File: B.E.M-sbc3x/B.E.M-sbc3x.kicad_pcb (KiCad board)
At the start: 2 copper layers, 7 parts, among them J1 Screw_Terminal_01x02, U1 6822, U2 6822, U3 MC68A09, U4 TC55257PL-12, U5 27256, U6 DM74S571

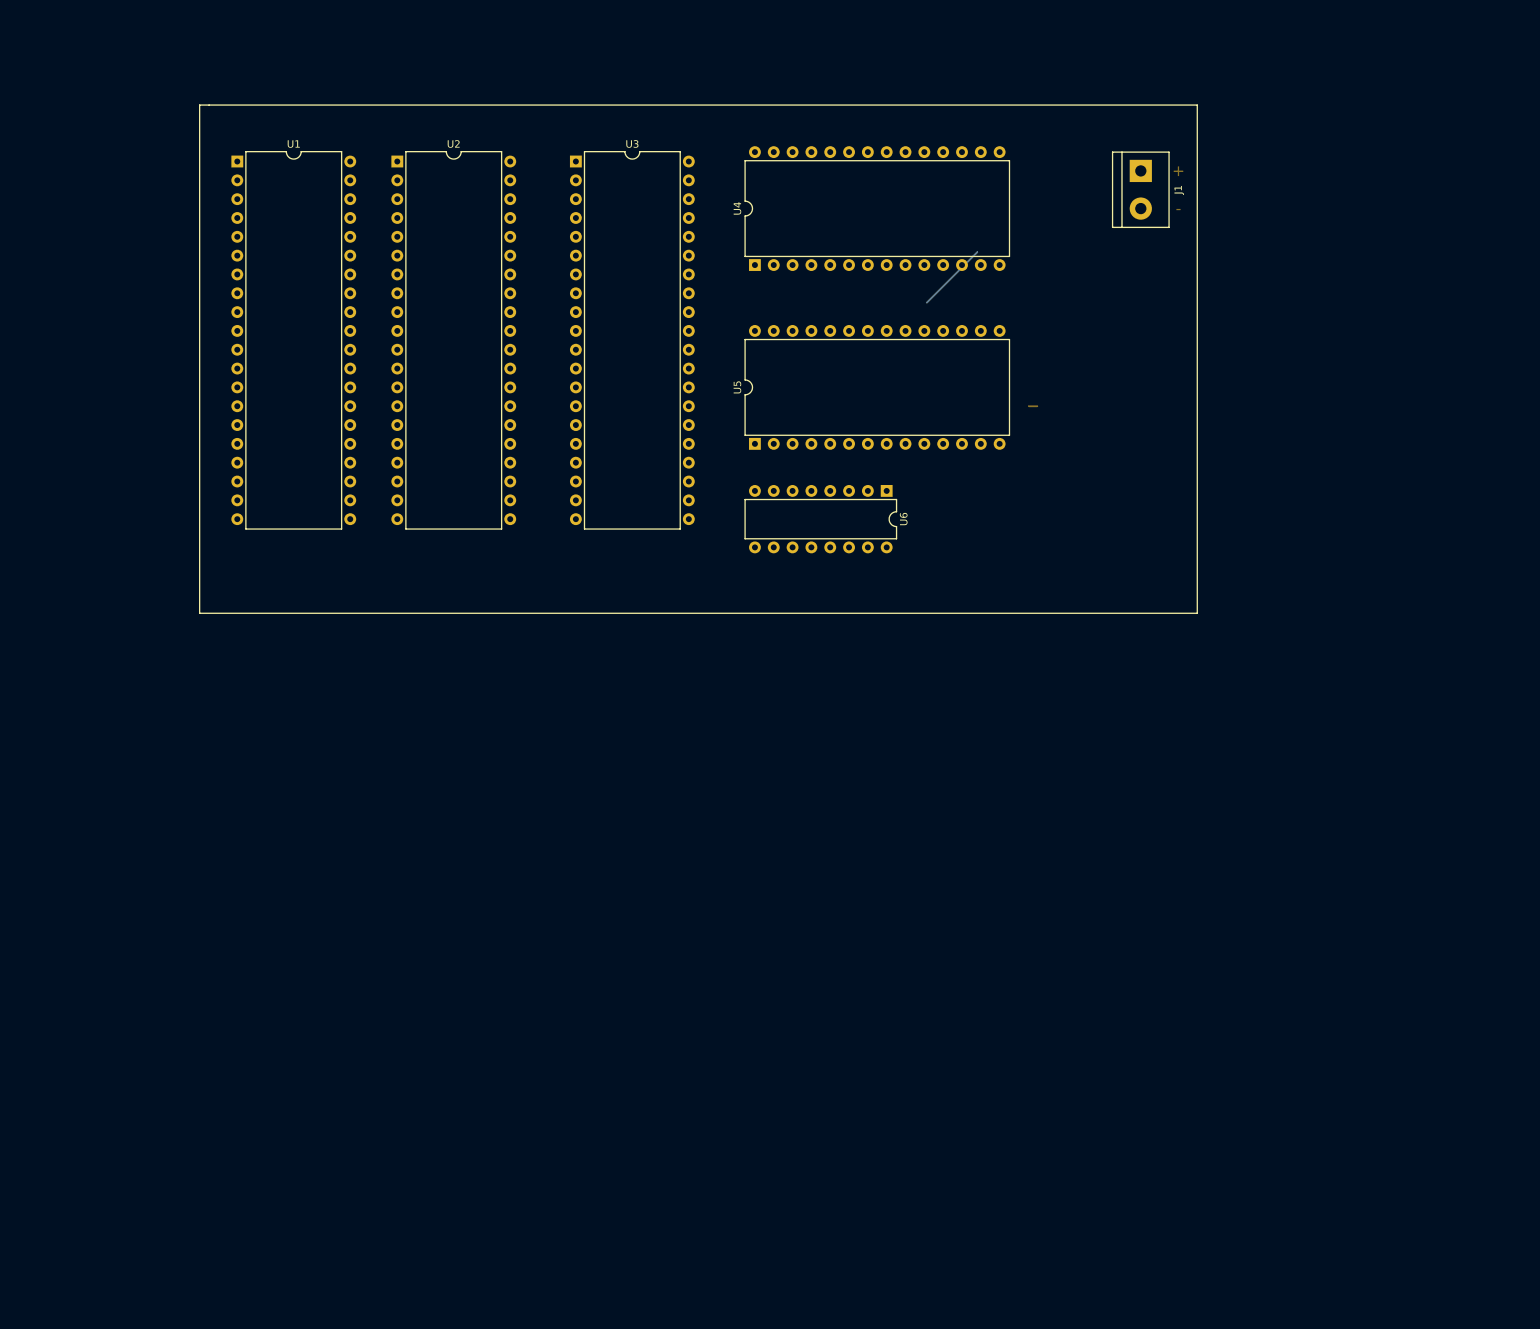
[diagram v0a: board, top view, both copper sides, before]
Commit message: Almost finnished with the schema and layout. Only some jumpers are not yet mapped out. For the PCB layout is only component placement is done, no routing
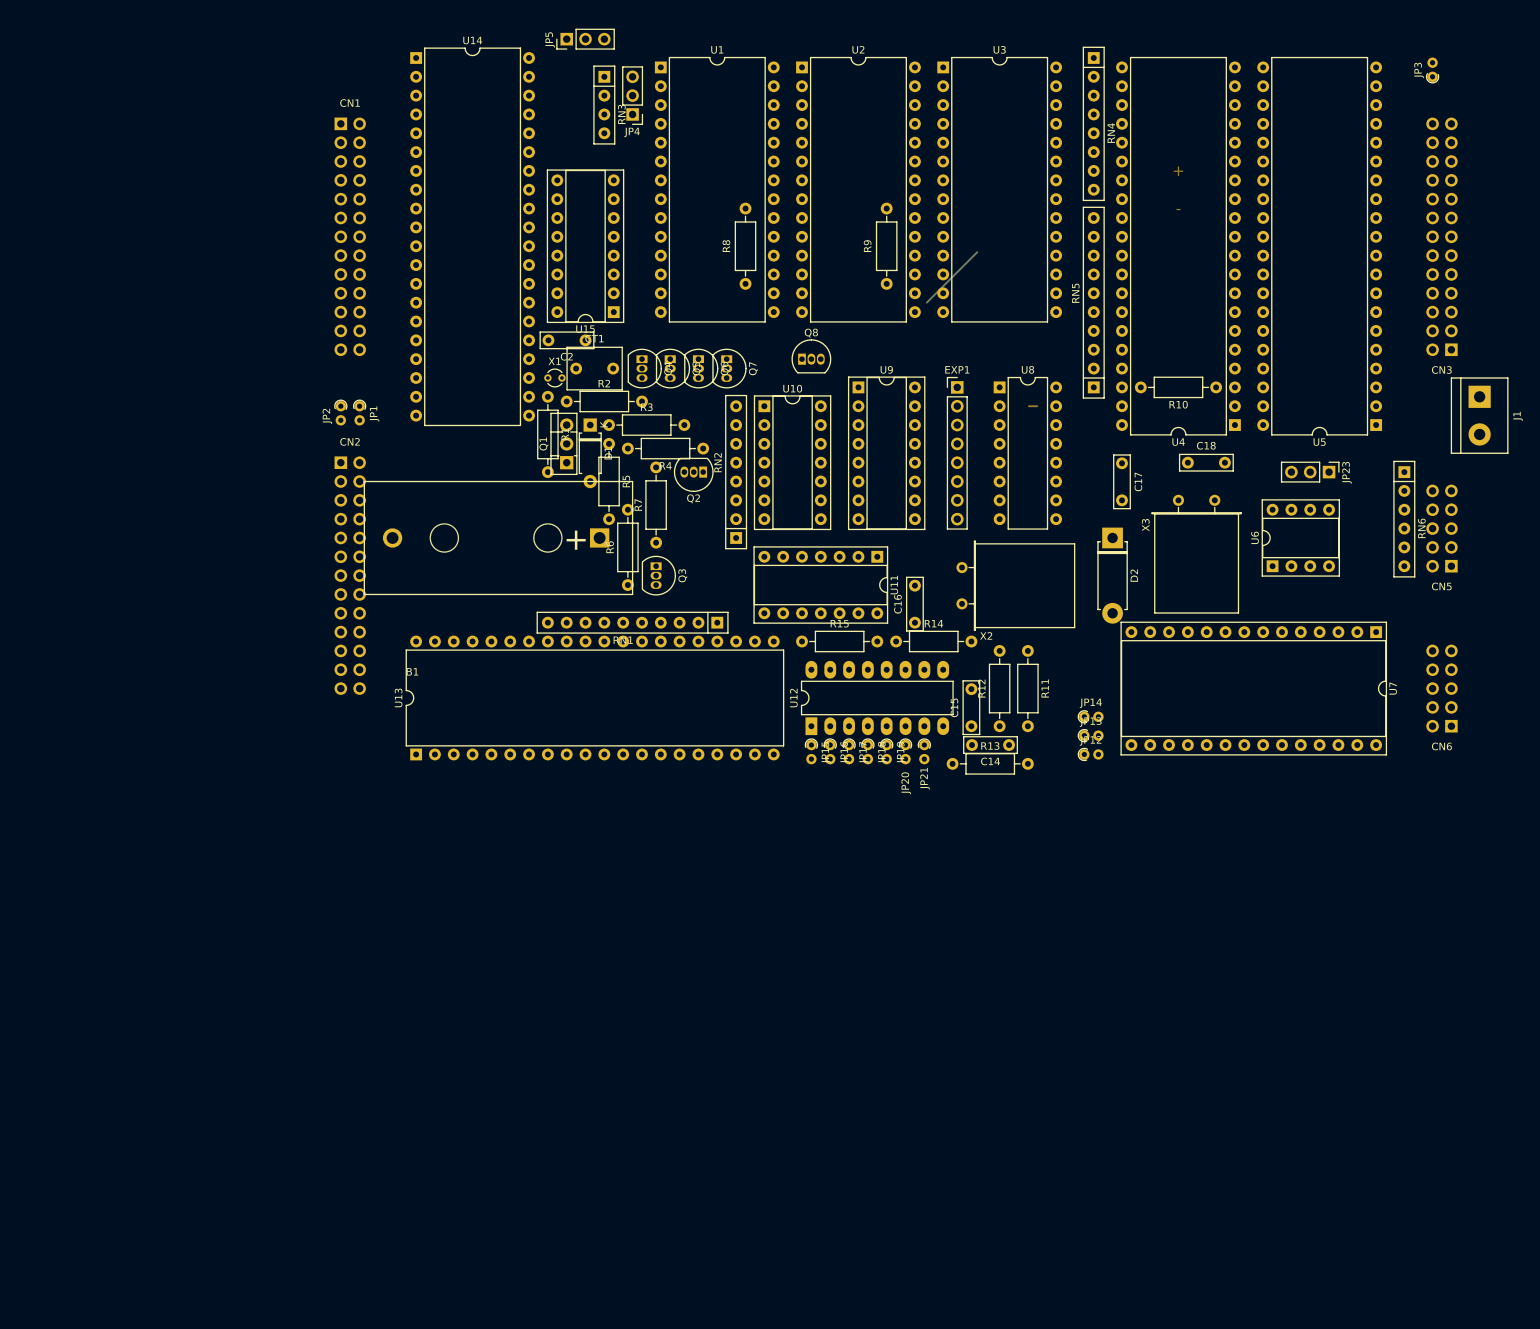
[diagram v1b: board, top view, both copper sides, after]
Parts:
- added B1: Battery_Cell, B.E.M:Battery_3.6v, F.Cu at (104.8, 90.2)
- added C14: 100n, Capacitor_THT:C_Rect_L7.0mm_W2.0mm_P5.00mm, F.Cu at (157.5, 118.1)
- added C15: 10n, Capacitor_THT:C_Rect_L7.0mm_W2.0mm_P5.00mm, F.Cu at (152.4, 115.6)
- added C16: 100pF, Capacitor_THT:C_Rect_L7.0mm_W2.0mm_P5.00mm, F.Cu at (144.8, 101.6)
- added C17: 22p, Capacitor_THT:C_Rect_L7.0mm_W2.0mm_P5.00mm, F.Cu at (172.7, 80.1)
- added C18: 22p, Capacitor_THT:C_Rect_L7.0mm_W2.0mm_P5.00mm, F.Cu at (181.6, 80.0)
- added C2: 22P, Capacitor_THT:C_Rect_L7.0mm_W2.0mm_P5.00mm, F.Cu at (100.3, 63.5)
- added CN1: Conn_02x13_Odd_Even, Connector_PinSocket_2.54mm:PinSocket_2x13_P2.54mm_Vertical, B.Cu at (67.3, 34.3)
- added CN2: Conn_02x13_Odd_Even, Connector_PinSocket_2.54mm:PinSocket_2x13_P2.54mm_Vertical, B.Cu at (67.3, 80.0)
- added CN3: Conn_02x13_Odd_Even, Connector_PinSocket_2.54mm:PinSocket_2x13_P2.54mm_Vertical, B.Cu at (217.2, 64.8)
- added CN5: Conn_02x05_Odd_Even, Connector_PinSocket_2.54mm:PinSocket_2x05_P2.54mm_Vertical, B.Cu at (217.2, 94.0)
- added CN6: Conn_02x05_Odd_Even, Connector_PinSocket_2.54mm:PinSocket_2x05_P2.54mm_Vertical, B.Cu at (217.2, 115.6)
- added CT1: 30pF, Capacitor_THT:C_Rect_L7.2mm_W5.5mm_P5.00mm_FKS2_FKP2_MKS2_MKP2, F.Cu at (99.1, 67.3)
- added D1: 1N4148, Diode_THT:D_A-405_P7.62mm_Horizontal, F.Cu at (101.0, 74.9)
- added D2: 1N4148, Diode_THT:D_5W_P10.16mm_Horizontal, F.Cu at (171.4, 90.2)
- added EXP1: Exp, Connector_PinHeader_2.54mm:PinHeader_1x08_P2.54mm_Vertical, F.Cu at (150.5, 69.8)
- added JP1: Jumper_NO_Small, Resistor_THT:R_Axial_DIN0204_L3.6mm_D1.6mm_P1.90mm_Vertical, F.Cu at (69.8, 72.4)
- added JP12: Jumper_NO_Small, Resistor_THT:R_Axial_DIN0204_L3.6mm_D1.6mm_P1.90mm_Vertical, F.Cu at (167.6, 119.4)
- added JP13: Jumper_NO_Small, Resistor_THT:R_Axial_DIN0204_L3.6mm_D1.6mm_P1.90mm_Vertical, F.Cu at (167.6, 116.8)
- added JP14: Jumper_NO_Small, Resistor_THT:R_Axial_DIN0204_L3.6mm_D1.6mm_P1.90mm_Vertical, F.Cu at (167.6, 114.3)
- added JP15: Jumper_NO_Small, Resistor_THT:R_Axial_DIN0204_L3.6mm_D1.6mm_P1.90mm_Vertical, F.Cu at (130.8, 118.1)
- added JP16: Jumper_NO_Small, Resistor_THT:R_Axial_DIN0204_L3.6mm_D1.6mm_P1.90mm_Vertical, F.Cu at (133.3, 118.1)
- added JP17: Jumper_NO_Small, Resistor_THT:R_Axial_DIN0204_L3.6mm_D1.6mm_P1.90mm_Vertical, F.Cu at (135.9, 118.1)
- added JP18: Jumper_NO_Small, Resistor_THT:R_Axial_DIN0204_L3.6mm_D1.6mm_P1.90mm_Vertical, F.Cu at (138.4, 118.1)
- added JP19: Jumper_NO_Small, Resistor_THT:R_Axial_DIN0204_L3.6mm_D1.6mm_P1.90mm_Vertical, F.Cu at (141.0, 118.1)
- added JP2: Jumper_NO_Small, Resistor_THT:R_Axial_DIN0204_L3.6mm_D1.6mm_P1.90mm_Vertical, F.Cu at (67.3, 72.4)
- added JP20: Jumper_NO_Small, Resistor_THT:R_Axial_DIN0204_L3.6mm_D1.6mm_P1.90mm_Vertical, F.Cu at (143.5, 118.1)
- added JP21: Jumper_NO_Small, Resistor_THT:R_Axial_DIN0204_L3.6mm_D1.6mm_P1.90mm_Vertical, F.Cu at (146.1, 118.1)
- added JP23: Jumper_3_Open, Connector_PinHeader_2.54mm:PinHeader_1x03_P2.54mm_Vertical, F.Cu at (200.7, 81.3)
- added JP3: Jumper_NO_Small, Resistor_THT:R_Axial_DIN0204_L3.6mm_D1.6mm_P1.90mm_Vertical, F.Cu at (214.6, 27.9)
- added JP4: Jumper_3_Open, Connector_PinHeader_2.54mm:PinHeader_1x03_P2.54mm_Vertical, F.Cu at (106.7, 33.0)
- added JP5: Jumper_3_Open, Connector_PinHeader_2.54mm:PinHeader_1x03_P2.54mm_Vertical, F.Cu at (97.8, 22.9)
- added Q1: BD136, Package_TO_SOT_THT:TO-126-3_Vertical, F.Cu at (97.8, 80.0)
- added Q2: BC556, Package_TO_SOT_THT:TO-92_Inline, F.Cu at (116.2, 81.3)
- added Q3: BC547, Package_TO_SOT_THT:TO-92_Inline, F.Cu at (109.9, 94.0)
- added Q4: BC547, Package_TO_SOT_THT:TO-92_Inline, F.Cu at (108.0, 66.0)
- added Q5: BC547, Package_TO_SOT_THT:TO-92_Inline, F.Cu at (111.8, 66.0)
- added Q6: BC547, Package_TO_SOT_THT:TO-92_Inline, F.Cu at (115.6, 66.0)
- added Q7: BC547, Package_TO_SOT_THT:TO-92_Inline, F.Cu at (119.4, 66.0)
- added Q8: BC547, Package_TO_SOT_THT:TO-92_Inline, F.Cu at (129.5, 66.0)
- added R1: 10K, Resistor_THT:R_Axial_DIN0207_L6.3mm_D2.5mm_P10.16mm_Horizontal, F.Cu at (95.2, 71.1)
- added R10: 3.3K, Resistor_THT:R_Axial_DIN0207_L6.3mm_D2.5mm_P10.16mm_Horizontal, F.Cu at (185.4, 69.8)
- added R11: 220K, Resistor_THT:R_Axial_DIN0207_L6.3mm_D2.5mm_P10.16mm_Horizontal, F.Cu at (160.0, 105.4)
- added R12: 22K, Resistor_THT:R_Axial_DIN0207_L6.3mm_D2.5mm_P10.16mm_Horizontal, F.Cu at (156.2, 115.6)
- added R13: 10K, Resistor_THT:R_Axial_DIN0207_L6.3mm_D2.5mm_P10.16mm_Horizontal, F.Cu at (149.9, 120.7)
- added R14: 3.3K, Resistor_THT:R_Axial_DIN0207_L6.3mm_D2.5mm_P10.16mm_Horizontal, F.Cu at (142.2, 104.1)
- added R15: 3.3K, Resistor_THT:R_Axial_DIN0207_L6.3mm_D2.5mm_P10.16mm_Horizontal, F.Cu at (129.5, 104.1)
- added R2: 1K, Resistor_THT:R_Axial_DIN0207_L6.3mm_D2.5mm_P10.16mm_Horizontal, F.Cu at (97.8, 71.8)
- added R3: 10K, Resistor_THT:R_Axial_DIN0207_L6.3mm_D2.5mm_P10.16mm_Horizontal, F.Cu at (103.5, 74.9)
- added R4: 10K, Resistor_THT:R_Axial_DIN0207_L6.3mm_D2.5mm_P10.16mm_Horizontal, F.Cu at (116.2, 78.1)
- added R5: 100, Resistor_THT:R_Axial_DIN0207_L6.3mm_D2.5mm_P10.16mm_Horizontal, F.Cu at (103.5, 77.5)
- added R6: 1K, Resistor_THT:R_Axial_DIN0207_L6.3mm_D2.5mm_P10.16mm_Horizontal, F.Cu at (106.0, 96.5)
- added R7: 1K, Resistor_THT:R_Axial_DIN0207_L6.3mm_D2.5mm_P10.16mm_Horizontal, F.Cu at (109.9, 90.8)
- added R8: 3.3K, Resistor_THT:R_Axial_DIN0207_L6.3mm_D2.5mm_P10.16mm_Horizontal, F.Cu at (121.9, 45.7)
- added R9: 3.3K, Resistor_THT:R_Axial_DIN0207_L6.3mm_D2.5mm_P10.16mm_Horizontal, F.Cu at (141.0, 45.7)
- added RN1: 10K, Resistor_THT:R_Array_SIP10, F.Cu at (118.1, 101.6)
- added RN2: 2k, Resistor_THT:R_Array_SIP8, F.Cu at (120.7, 90.2)
- added RN3: 3.3K, Resistor_THT:R_Array_SIP4, F.Cu at (102.9, 27.9)
- added RN4: 10K, Resistor_THT:R_Array_SIP8, F.Cu at (168.9, 25.4)
- added RN5: 10K, Resistor_THT:R_Array_SIP10, F.Cu at (168.9, 69.8)
- added RN6: 3.3K, Resistor_THT:R_Array_SIP6, F.Cu at (210.8, 81.3)
- added U1: TC55257PL-12, Package_DIP:DIP-28_W15.24mm, F.Cu at (110.5, 26.7)
- added U10: 74LS00, Package_DIP:DIP-14_W7.62mm_Socket, F.Cu at (124.5, 72.4)
- added U11: 74HC04, Package_DIP:DIP-14_W7.62mm_Socket, F.Cu at (139.7, 92.7)
- added U12: CD4060BCN, Package_DIP:DIP-16_W7.62mm_LongPads, F.Cu at (130.8, 115.6)
- added U13: 6822, Package_DIP:DIP-40_W15.24mm, F.Cu at (77.5, 119.4)
- added U15: MM58274BN, Package_DIP:DIP-16_W7.62mm_Socket, F.Cu at (104.1, 59.7)
- added U6: TL7705ACPSR, Package_DIP:DIP-8_W7.62mm_Socket, F.Cu at (193.0, 94.0)
- added U7: INS2651, Package_DIP:DIP-28_W15.24mm_Socket, F.Cu at (207.0, 102.9)
- added U9: 74LS42, Package_DIP:DIP-16_W7.62mm_Socket, F.Cu at (137.2, 69.8)
- added X1: 32.768, Crystal:Crystal_DS26_D2.0mm_L6.0mm_Vertical, F.Cu at (95.2, 68.6)
- added X2: 5.0688, Crystal:Crystal_HC18-U_Horizontal, F.Cu at (151.1, 99.1)
- added X3: 4.000, Crystal:Crystal_HC18-U_Horizontal, F.Cu at (180.3, 85.1)
- moved U5 157.7 mm to (207.0, 74.9), turned to 180 degrees
- moved U4 95.8 mm to (188.0, 74.9), turned to 180 degrees
- moved U3 56.8 mm to (148.6, 26.7), turned to 0 degrees
- moved J1 54.9 mm to (221.0, 71.1)
- moved U2 27.4 mm to (129.5, 26.7), turned to 0 degrees
- moved U8 20.7 mm to (156.2, 69.8), turned to 0 degrees
- moved U14 14.2 mm to (77.5, 25.4)
- renumbered U2 to U14, U4 to U2, U5 to U3, U3 to U4, U1 to U5, U6 to U8
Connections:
- U14 pad 21: (no net) -> /C5-4
- U14 pad 22: (no net) -> /RW
- U14 pad 23: (no net) -> Net-(U14-Pad23)
- U14 pad 24: (no net) -> +5V
- U14 pad 25: (no net) -> /E
- U14 pad 35: (no net) -> /A3
- U14 pad 36: (no net) -> /A2
- U14 pad 37: (no net) -> /A1
- U14 pad 38: (no net) -> /A0
- U2 pad 20: (no net) -> Net-(Q8-Pad3)
- U2 pad 22: (no net) -> Net-(U1-Pad22)
- U2 pad 27: (no net) -> Net-(JP4-Pad3)
- U3 pad 20: (no net) -> Net-(U3-Pad20)
- U4 pad 2: (no net) -> /C5-3
- U4 pad 23: (no net) -> /A15
- U4 pad 3: (no net) -> /C5-4
- U4 pad 32: (no net) -> /RW
- U4 pad 33: (no net) -> +5V
- U4 pad 34: (no net) -> /E
- U4 pad 36: (no net) -> Net-(R10-Pad2)
- U4 pad 38: (no net) -> Net-(C17-Pad1)
- U4 pad 39: (no net) -> Net-(C18-Pad1)
- U4 pad 4: (no net) -> /C5-2
- U4 pad 40: (no net) -> /C5-5
- U5 pad 21: (no net) -> /C5-4
- U5 pad 22: (no net) -> /RW
- U5 pad 23: (no net) -> Net-(U5-Pad23)
- U5 pad 24: (no net) -> +5V
- U5 pad 25: (no net) -> /E
- U5 pad 35: (no net) -> /A3
- U5 pad 36: (no net) -> /A2
- U5 pad 37: (no net) -> /A1
- U5 pad 38: (no net) -> /A0
- U8 pad 1: (no net) -> /A13
- U8 pad 10: (no net) -> Net-(EXP1-Pad4)
- U8 pad 11: (no net) -> Net-(EXP1-Pad3)
- U8 pad 12: (no net) -> Net-(EXP1-Pad2)
- U8 pad 13: (no net) -> GND
- U8 pad 14: (no net) -> /A15
- U8 pad 15: (no net) -> /A14
- U8 pad 2: (no net) -> /A12
- U8 pad 3: (no net) -> /A11
- U8 pad 4: (no net) -> /A10
- U8 pad 6: (no net) -> /A8
- U8 pad 7: (no net) -> /A9
- U8 pad 9: (no net) -> Net-(EXP1-Pad5)
